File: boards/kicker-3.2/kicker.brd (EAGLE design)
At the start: 141 x 146.1 mm, 150 parts, among them J1 B2PS-VH(LF)(SN), J2 B2PS-VH(LF)(SN), J3 B2PS-VH(LF)(SN), J4 HFW8R-1ST, J5 2-PIN_2MM-H, J6 3-PIN_2MM-H, J7 !BTN_KCK_PRE_EXT, J8 !BTN_CHP_PRE_EXT, J9 !BTN_CHG_PRE_EXT, Q1 ATP302ATPAK, Q10 BSS806NSOT-23-3, Q2 IRFS4227, Q3 IXGK400N30A3, Q4 IXGK400N30A3, Q5 BSS127, Q6 AOD1N60, Q7 BSS127, Q8 BSS127, Q9 BSS127, T1 DA203X-ALDA2034, U1 MPM3620GQV-P, U2 15V, U3 LT3751FE, U4 IX4427N, U5 AT32ATQFP44, U6 ADUM7441ARQZ-RL7, U7 ADUM7441CRQZ-RL7

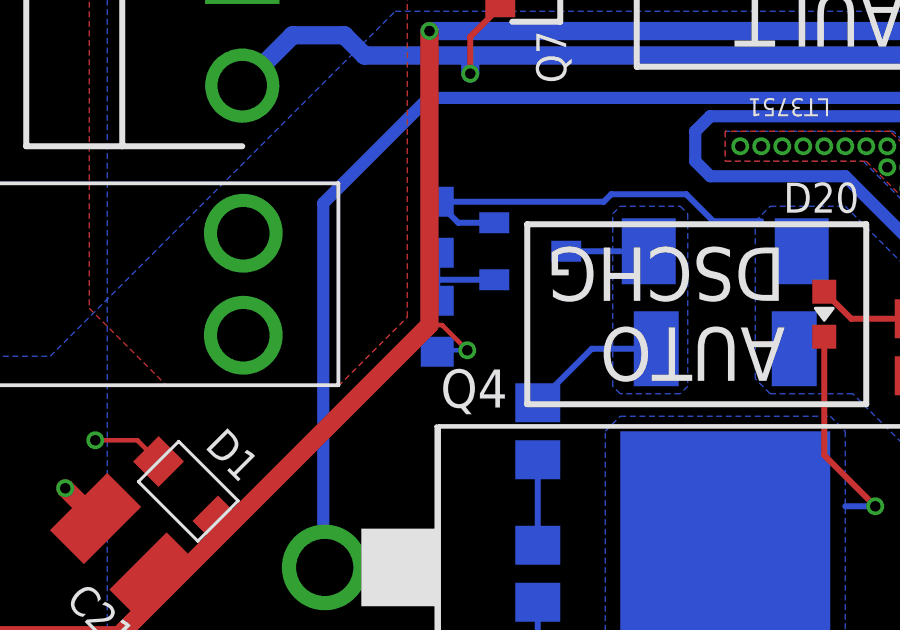
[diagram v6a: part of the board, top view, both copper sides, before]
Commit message: added cap to AOD gate add delay during clamping bias
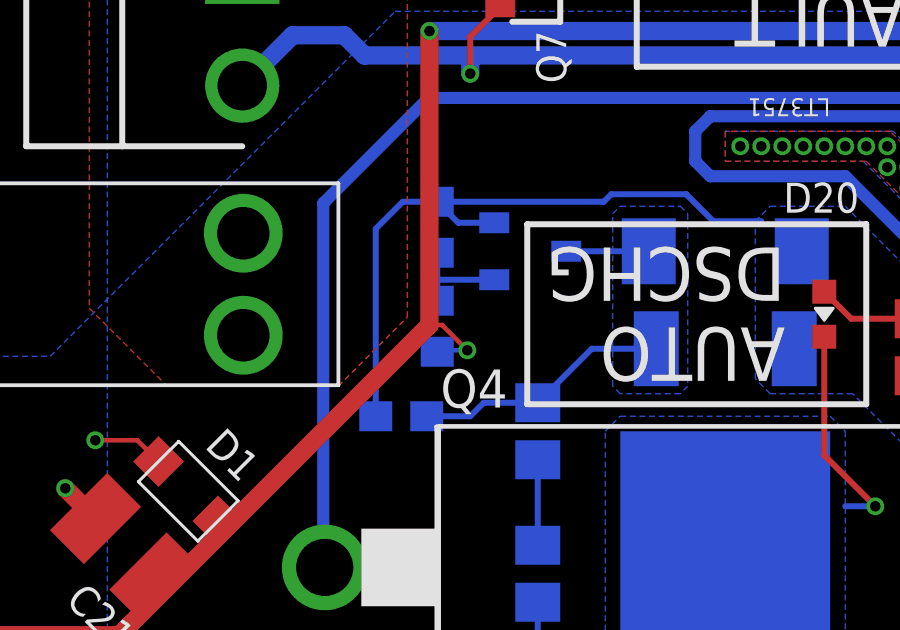
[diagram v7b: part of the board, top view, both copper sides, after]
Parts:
- added C38: 0.1uF 50V, rcl:C0603
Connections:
- net GND: now also C38.1
- net QUICK_DISCHARGE: now also C38.2
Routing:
- net GND: track 208.9 -> 217.6 mm
- net QUICK_DISCHARGE: track 6.50 -> 10.4 mm
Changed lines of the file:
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@@
 <?xml version="1.0" encoding="utf-8"?>
 <!DOCTYPE eagle SYSTEM "eagle.dtd">
-<eagle version="9.4.2">
+<eagle version="9.3.2">
 <drawing>
 <settings>
@@
 <grid distance="0.1" unitdist="mm" unit="mm" style="lines" multiple="1" display="yes" altdistance="0.05" altunitdist="mm" altunit="mm"/>
 <layers>
-<layer number="1" name="Top" color="4" fill="1" visible="yes" active="yes"/>
+<layer number="1" name="Top" color="4" fill="1" visible="no" active="yes"/>
 <layer number="2" name="Route2" color="1" fill="3" visible="no" active="no"/>
 <layer number="3" name="Route3" color="4" fill="3" visible="no" active="no"/>
@@
 <layer number="19" name="Unrouted" color="6" fill="1" visible="yes" active="yes"/>
 <layer number="20" name="Dimension" color="15" fill="1" visible="yes" active="yes"/>
-<layer number="21" name="tPlace" color="7" fill="1" visible="yes" active="yes"/>
+<layer number="21" name="tPlace" color="7" fill="1" visible="no" active="yes"/>
 <layer number="22" name="bPlace" color="7" fill="1" visible="yes" active="yes"/>
-<layer number="23" name="tOrigins" color="15" fill="1" visible="yes" active="yes"/>
+<layer number="23" name="tOrigins" color="15" fill="1" visible="no" active="yes"/>
 <layer number="24" name="bOrigins" color="15" fill="1" visible="yes" active="yes"/>
-<layer number="25" name="tNames" color="7" fill="1" visible="yes" active="yes"/>
+<layer number="25" name="tNames" color="7" fill="1" visible="no" active="yes"/>
 <layer number="26" name="bNames" color="7" fill="1" visible="yes" active="yes"/>
 <layer number="27" name="tValues" color="7" fill="1" visible="no" active="yes"/>
@@
 <layer number="37" name="tTest" color="7" fill="1" visible="no" active="yes"/>
 <layer number="38" name="bTest" color="7" fill="1" visible="no" active="yes"/>
-<layer number="39" name="tKeepout" color="4" fill="11" visible="yes" active="yes"/>
+<layer number="39" name="tKeepout" color="4" fill="11" visible="no" active="yes"/>
 <layer number="40" name="bKeepout" color="1" fill="11" visible="yes" active="yes"/>
-<layer number="41" name="tRestrict" color="4" fill="10" visible="yes" active="yes"/>
+<layer number="41" name="tRestrict" color="4" fill="10" visible="no" active="yes"/>
 <layer number="42" name="bRestrict" color="1" fill="10" visible="yes" active="yes"/>
 <layer number="43" name="vRestrict" color="2" fill="10" visible="no" active="yes"/>
 <layer number="44" name="Drills" color="7" fill="1" visible="no" active="yes"/>
-<layer number="45" name="Holes" color="7" fill="1" visible="no" active="yes"/>
+<layer number="45" name="Holes" color="7" fill="1" visible="yes" active="yes"/>
 <layer number="46" name="Milling" color="3" fill="1" visible="no" active="yes"/>
 <layer number="47" name="Measures" color="7" fill="1" visible="no" active="yes"/>
@@
 <layer number="49" name="Reference" color="7" fill="1" visible="no" active="yes"/>
 <layer number="50" name="dxf" color="7" fill="1" visible="no" active="no"/>
-<layer number="51" name="tDocu" color="7" fill="1" visible="yes" active="yes"/>
+<layer number="51" name="tDocu" color="7" fill="1" visible="no" active="yes"/>
 <layer number="52" name="bDocu" color="7" fill="1" visible="yes" active="yes"/>
 <layer number="53" name="tGND_GNDA" color="7" fill="9" visible="no" active="no"/>
@@
 <attribute name="SPICEPREFIX" value="R" x="-39.7" y="-18" size="1.778" layer="27" rot="R180" display="off"/>
 <attribute name="VALUE" x="-39.065" y="-16.095" size="1.27" layer="27" rot="R180"/>
+</element>
+<element name="C38" library="rcl" library_urn="urn:adsk.eagle:library:334" package="C0603" package3d_urn="urn:adsk.eagle:package:23616/2" value="0.1uF 50V" x="-9.3" y="59.5" smashed="yes" rot="MR180">
+<attribute name="NAME" x="-9.935" y="58.865" size="1" layer="26" font="vector" rot="MR180"/>
+<attribute name="SPICEPREFIX" value="C" x="-9.3" y="59.5" size="1.778" layer="28" rot="MR180" display="off"/>
+<attribute name="VALUE" x="-9.935" y="61.405" size="1.27" layer="28" rot="MR180"/>
 </element>
 </elements>
@@
 <wire x1="54.8525" y1="33.8969" x2="55.5278" y2="34.5722" width="0.2" layer="1"/>
 <via x="55.5278" y="34.5722" extent="1-16" drill="0.35"/>
+<contactref element="C38" pad="1"/>
+<wire x1="-10.15" y1="59.5" x2="-10.15" y2="65.75" width="0.2" layer="16"/>
+<wire x1="-9.25" y1="66.65" x2="-8.1" y2="66.65" width="0.2" layer="16"/>
+<wire x1="-10.15" y1="65.75" x2="-9.25" y2="66.65" width="0.2" layer="16"/>
 </signal>
 <signal name="CHARGE">
@@
 </polygon>
 <wire x1="-3.8" y1="65" x2="-2" y2="65" width="0.2" layer="16"/>
+<contactref element="C38" pad="2"/>
+<wire x1="-4.75" y1="59.95" x2="-6.55" y2="59.95" width="0.2" layer="16"/>
+<wire x1="-7" y1="59.5" x2="-8.45" y2="59.5" width="0.2" layer="16"/>
+<wire x1="-6.55" y1="59.95" x2="-7" y2="59.5" width="0.2" layer="16"/>
 </signal>
 <signal name="QD_GATE_CTRL">
